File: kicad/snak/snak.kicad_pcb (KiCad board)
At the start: 2 copper layers, 115.6 x 99.6 mm, 70 parts

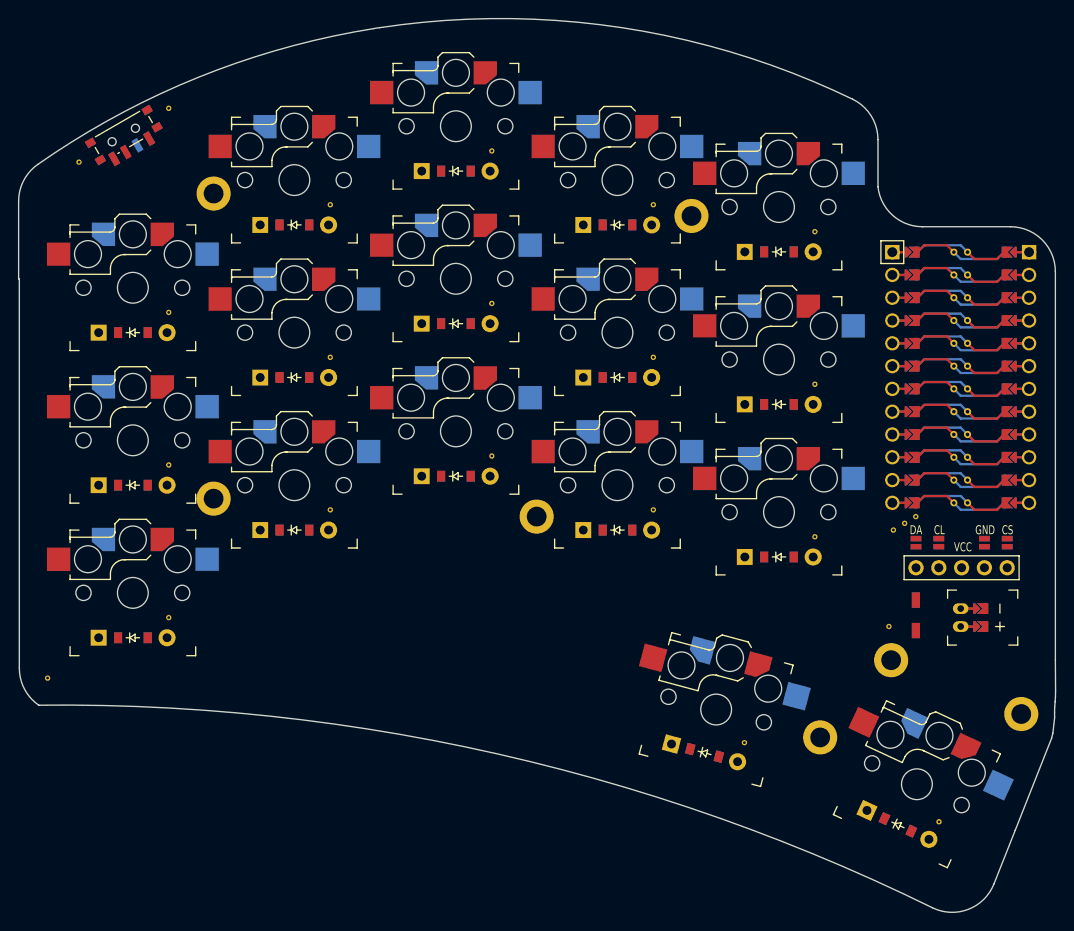
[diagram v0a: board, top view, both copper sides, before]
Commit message: changed the top and bottom curves to a single polygon
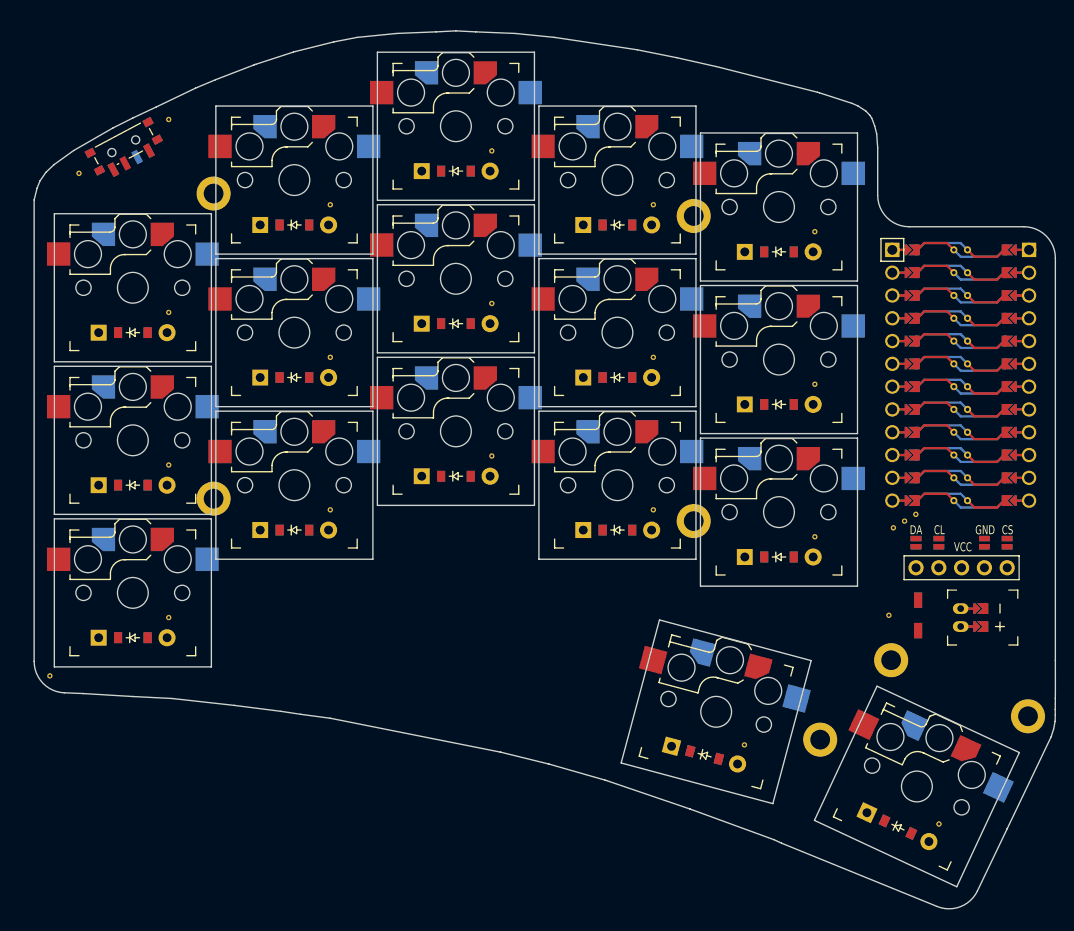
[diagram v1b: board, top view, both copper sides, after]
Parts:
- removed the REF** at (184.8, 93.0)
- removed the REF** at (168.2, 116.7)
- removed the REF** at (186.0, 92.2)
- removed the REF** at (189.8, 125.5)
- removed the REF** at (104.0, 46.0)
- removed the REF** at (94.0, 52.0)
- removed the REF** at (90.5, 109.5)
- removed the REF** at (184.2, 103.8)
- removed the REF** at (187.2, 91.5)
- added REF**: VIA-0.6mm, VIA-0.6mm, F.Cu at (184.8, 92.8)
- added REF**: VIA-0.6mm, VIA-0.6mm, F.Cu at (168.2, 116.9)
- added REF**: VIA-0.6mm, VIA-0.6mm, F.Cu at (186.0, 92.0)
- added REF**: VIA-0.6mm, VIA-0.6mm, F.Cu at (189.8, 125.8)
- added REF**: VIA-0.6mm, VIA-0.6mm, F.Cu at (104.0, 47.2)
- added REF**: VIA-0.6mm, VIA-0.6mm, F.Cu at (94.0, 53.2)
- added REF**: VIA-0.6mm, VIA-0.6mm, F.Cu at (90.8, 109.2)
- added REF**: VIA-0.6mm, VIA-0.6mm, F.Cu at (184.2, 102.5)
- added REF**: VIA-0.6mm, VIA-0.6mm, F.Cu at (187.2, 91.2)
- moved H4 17.5 mm to (162.5, 92.0)
- moved SW1 1.25 mm to (99.0, 50.2), turned to 118 degrees
- moved H7 0.79 mm to (199.8, 113.8)
- moved ? 0.25 mm to (187.5, 102.5)
- moved D16 0.25 mm to (163.7, 118.1)
- moved D17 0.25 mm to (185.3, 126.1)
- moved H3 0.25 mm to (162.5, 58.0)
- moved H5 0.25 mm to (176.6, 116.4)
- moved MCU1 0.25 mm to (192.2, 75.8)
- moved S16 0.25 mm to (165.0, 113.2)
- moved S17 0.25 mm to (187.4, 121.6)
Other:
- board size 115.6 x 99.6 mm -> 113.8 x 97.8 mm

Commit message: add via for oled gnd
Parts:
- added REF**: VIA-0.6mm, VIA-0.6mm, F.Cu at (194.9, 92.0)
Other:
- outline, holes or cut-outs redrawn
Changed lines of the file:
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@@
       (pad 1 thru_hole circle (at 0 0) (size 0.6 0.6) (drill 0.3) (layers *.Cu) (zone_connect 2) (net 20 "P7"))
+      )
+      (module VIA-0.6mm (layer F.Cu)
+      (at 194.9 92 0)
+      (fp_text reference REF** (at 0 1.4) (layer F.SilkS) hide (effects (font (size 1 1) (thickness 0.15))))
+      (fp_text value VIA-0.6mm (at 0 -1.4) (layer F.Fab) hide (effects (font (size 1 1) (thickness 0.15))))
+      (pad 1 thru_hole circle (at 0 0) (size 0.6 0.6) (drill 0.3) (layers *.Cu) (zone_connect 2) (net 2 "GND"))
       )
             (module PG1350 (layer F.Cu)
@@
 (gr_arc (start 145.45718132399764 122.4562241087232) (end 146.41926002399765 119.0910488087232) (angle -2.100604721951811) (layer Edge.Cuts) (width 0.15))
 (gr_arc (start 140.2553549312661 121.17331056590517) (end 141.09343903126612 117.77513236590516) (angle -2.5939778102701183) (layer Edge.Cuts) (width 0.15))
-(gr_line (start 91.25 108.25) (end 108.75 108.25) (angle 90) (layer Edge.Cuts) (width 0.15))
-(gr_line (start 108.75 108.25) (end 108.75 91.75) (angle 90) (layer Edge.Cuts) (width 0.15))
-(gr_line (start 108.75 91.75) (end 91.25 91.75) (angle 90) (layer Edge.Cuts) (width 0.15))
-(gr_line (start 91.25 91.75) (end 91.25 108.25) (angle 90) (layer Edge.Cuts) (width 0.15))
-(gr_line (start 91.25 91.25) (end 108.75 91.25) (angle 90) (layer Edge.Cuts) (width 0.15))
-(gr_line (start 108.75 91.25) (end 108.75 74.75) (angle 90) (layer Edge.Cuts) (width 0.15))
-(gr_line (start 108.75 74.75) (end 91.25 74.75) (angle 90) (layer Edge.Cuts) (width 0.15))
-(gr_line (start 91.25 74.75) (end 91.25 91.25) (angle 90) (layer Edge.Cuts) (width 0.15))
-(gr_line (start 91.25 74.25) (end 108.75 74.25) (angle 90) (layer Edge.Cuts) (width 0.15))
-(gr_line (start 108.75 74.25) (end 108.75 57.75) (angle 90) (layer Edge.Cuts) (width 0.15))
-(gr_line (start 108.75 57.75) (end 91.25 57.75) (angle 90) (layer Edge.Cuts) (width 0.15))
-(gr_line (start 91.25 57.75) (end 91.25 74.25) (angle 90) (layer Edge.Cuts) (width 0.15))
-(gr_line (start 109.25 96.25) (end 126.75 96.25) (angle 90) (layer Edge.Cuts) (width 0.15))
-(gr_line (start 126.75 96.25) (end 126.75 79.75) (angle 90) (layer Edge.Cuts) (width 0.15))
-(gr_line (start 126.75 79.75) (end 109.25 79.75) (angle 90) (layer Edge.Cuts) (width 0.15))
-(gr_line (start 109.25 79.75) (end 109.25 96.25) (angle 90) (layer Edge.Cuts) (width 0.15))
-(gr_line (start 109.25 79.25) (end 126.75 79.25) (angle 90) (layer Edge.Cuts) (width 0.15))
-(gr_line (start 126.75 79.25) (end 126.75 62.75) (angle 90) (layer Edge.Cuts) (width 0.15))
-(gr_line (start 126.75 62.75) (end 109.25 62.75) (angle 90) (layer Edge.Cuts) (width 0.15))
-(gr_line (start 109.25 62.75) (end 109.25 79.25) (angle 90) (layer Edge.Cuts) (width 0.15))
-(gr_line (start 109.25 62.25) (end 126.75 62.25) (angle 90) (layer Edge.Cuts) (width 0.15))
-(gr_line (start 126.75 62.25) (end 126.75 45.75) (angle 90) (layer Edge.Cuts) (width 0.15))
-(gr_line (start 126.75 45.75) (end 109.25 45.75) (angle 90) (layer Edge.Cuts) (width 0.15))
-(gr_line (start 109.25 45.75) (end 109.25 62.25) (angle 90) (layer Edge.Cuts) (width 0.15))
-(gr_line (start 127.25 90.25) (end 144.75 90.25) (angle 90) (layer Edge.Cuts) (width 0.15))
-(gr_line (start 144.75 90.25) (end 144.75 73.75) (angle 90) (layer Edge.Cuts) (width 0.15))
-(gr_line (start 144.75 73.75) (end 127.25 73.75) (angle 90) (layer Edge.Cuts) (width 0.15))
-(gr_line (start 127.25 73.75) (end 127.25 90.25) (angle 90) (layer Edge.Cuts) (width 0.15))
-(gr_line (start 127.25 73.25) (end 144.75 73.25) (angle 90) (layer Edge.Cuts) (width 0.15))
-(gr_line (start 144.75 73.25) (end 144.75 56.75) (angle 90) (layer Edge.Cuts) (width 0.15))
-(gr_line (start 144.75 56.75) (end 127.25 56.75) (angle 90) (layer Edge.Cuts) (width 0.15))
-(gr_line (start 127.25 56.75) (end 127.25 73.25) (angle 90) (layer Edge.Cuts) (width 0.15))
-(gr_line (start 127.25 56.25) (end 144.75 56.25) (angle 90) (layer Edge.Cuts) (width 0.15))
-(gr_line (start 144.75 56.25) (end 144.75 39.75) (angle 90) (layer Edge.Cuts) (width 0.15))
-(gr_line (start 144.75 39.75) (end 127.25 39.75) (angle 90) (layer Edge.Cuts) (width 0.15))
-(gr_line (start 127.25 39.75) (end 127.25 56.25) (angle 90) (layer Edge.Cuts) (width 0.15))
-(gr_line (start 145.25 96.25) (end 162.75 96.25) (angle 90) (layer Edge.Cuts) (width 0.15))
-(gr_line (start 162.75 96.25) (end 162.75 79.75) (angle 90) (layer Edge.Cuts) (width 0.15))
-(gr_line (start 162.75 79.75) (end 145.25 79.75) (angle 90) (layer Edge.Cuts) (width 0.15))
-(gr_line (start 145.25 79.75) (end 145.25 96.25) (angle 90) (layer Edge.Cuts) (width 0.15))
-(gr_line (start 145.25 79.25) (end 162.75 79.25) (angle 90) (layer Edge.Cuts) (width 0.15))
-(gr_line (start 162.75 79.25) (end 162.75 62.75) (angle 90) (layer Edge.Cuts) (width 0.15))
-(gr_line (start 162.75 62.75) (end 145.25 62.75) (angle 90) (layer Edge.Cuts) (width 0.15))
-(gr_line (start 145.25 62.75) (end 145.25 79.25) (angle 90) (layer Edge.Cuts) (width 0.15))
-(gr_line (start 145.25 62.25) (end 162.75 62.25) (angle 90) (layer Edge.Cuts) (width 0.15))
-(gr_line (start 162.75 62.25) (end 162.75 45.75) (angle 90) (layer Edge.Cuts) (width 0.15))
-(gr_line (start 162.75 45.75) (end 145.25 45.75) (angle 90) (layer Edge.Cuts) (width 0.15))
-(gr_line (start 145.25 45.75) (end 145.25 62.25) (angle 90) (layer Edge.Cuts) (width 0.15))
-(gr_line (start 163.25 99.25) (end 180.75 99.25) (angle 90) (layer Edge.Cuts) (width 0.15))
-(gr_line (start 180.75 99.25) (end 180.75 82.75) (angle 90) (layer Edge.Cuts) (width 0.15))
-(gr_line (start 180.75 82.75) (end 163.25 82.75) (angle 90) (layer Edge.Cuts) (width 0.15))
-(gr_line (start 163.25 82.75) (end 163.25 99.25) (angle 90) (layer Edge.Cuts) (width 0.15))
-(gr_line (start 163.25 82.25) (end 180.75 82.25) (angle 90) (layer Edge.Cuts) (width 0.15))
-(gr_line (start 180.75 82.25) (end 180.75 65.75) (angle 90) (layer Edge.Cuts) (width 0.15))
-(gr_line (start 180.75 65.75) (end 163.25 65.75) (angle 90) (layer Edge.Cuts) (width 0.15))
-(gr_line (start 163.25 65.75) (end 163.25 82.25) (angle 90) (layer Edge.Cuts) (width 0.15))
-(gr_line (start 163.25 65.25) (end 180.75 65.25) (angle 90) (layer Edge.Cuts) (width 0.15))
-(gr_line (start 180.75 65.25) (end 180.75 48.75) (angle 90) (layer Edge.Cuts) (width 0.15))
-(gr_line (start 180.75 48.75) (end 163.25 48.75) (angle 90) (layer Edge.Cuts) (width 0.15))
-(gr_line (start 163.25 48.75) (end 163.25 65.25) (angle 90) (layer Edge.Cuts) (width 0.15))
-(gr_line (start 154.4128919 118.9542214) (end 171.3165939 123.4835547) (angle 90) (layer Edge.Cuts) (width 0.15))
-(gr_line (start 171.3165939 123.4835547) (end 175.5871081 107.5457786) (angle 90) (layer Edge.Cuts) (width 0.15))
-(gr_line (start 175.5871081 107.5457786) (end 158.6834061 103.0164453) (angle 90) (layer Edge.Cuts) (width 0.15))
-(gr_line (start 158.6834061 103.0164453) (end 154.4128919 118.9542214) (angle 90) (layer Edge.Cuts) (width 0.15))
-(gr_line (start 175.95126100000002 125.35200309999998) (end 191.8116473 132.74782259999998) (angle 90) (layer Edge.Cuts) (width 0.15))
-(gr_line (start 191.8116473 132.74782259999998) (end 198.7848486 117.79374409999998) (angle 90) (layer Edge.Cuts) (width 0.15))
-(gr_line (start 198.7848486 117.79374409999998) (end 182.92446230000002 110.39792459999998) (angle 90) (layer Edge.Cuts) (width 0.15))
-(gr_line (start 182.92446230000002 110.39792459999998) (end 175.95126100000002 125.35200309999998) (angle 90) (layer Edge.Cuts) (width 0.15))
 (gr_line (start 91.25 108.25) (end 108.75 108.25) (angle 90) (layer Eco1.User) (width 0.15))
 (gr_line (start 108.75 108.25) (end 108.75 91.75) (angle 90) (layer Eco1.User) (width 0.15))

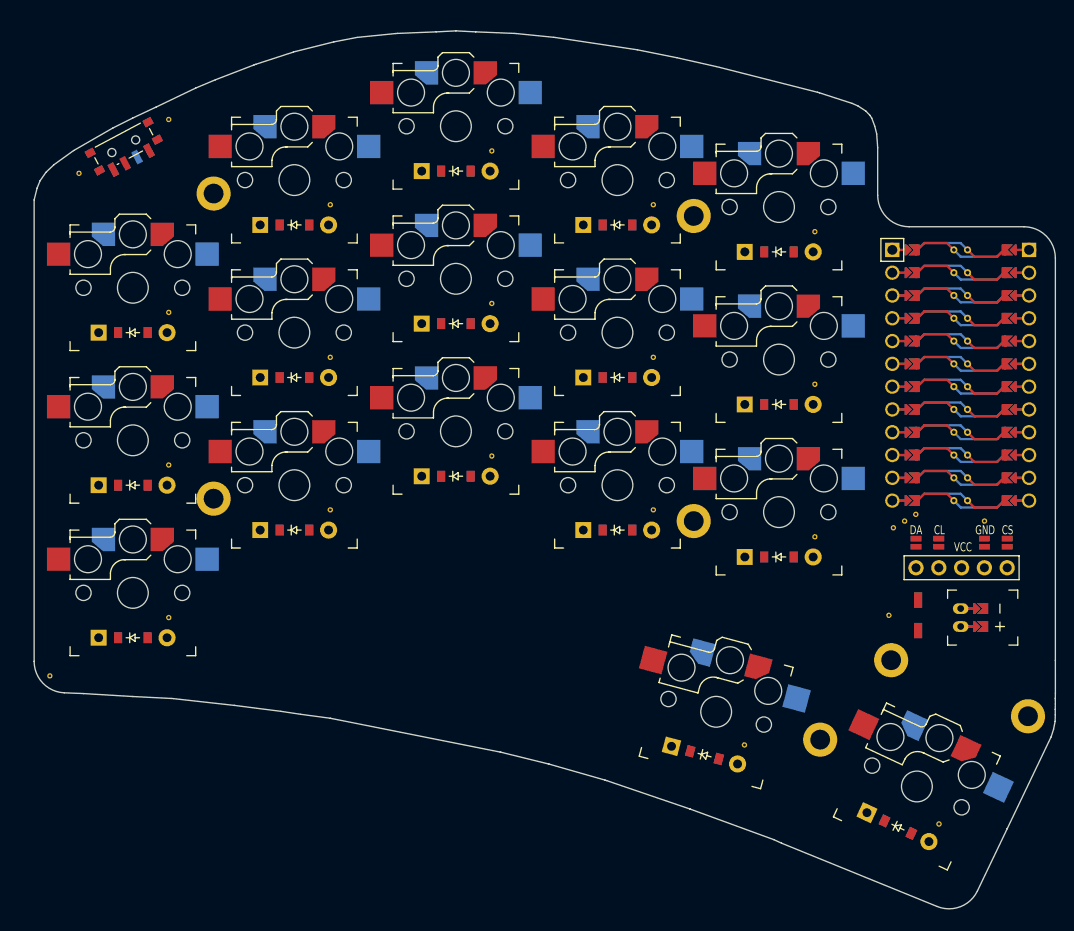
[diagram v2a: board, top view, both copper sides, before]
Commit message: update config with circle intersect
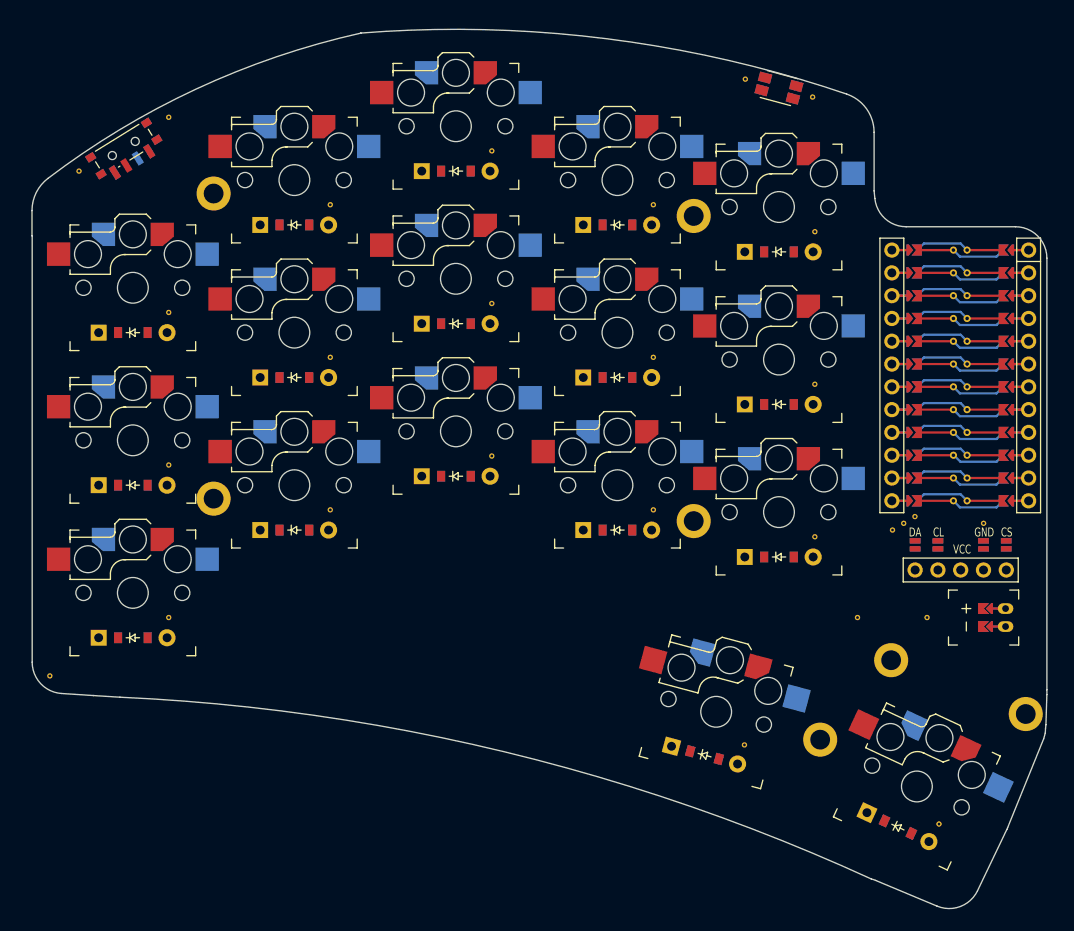
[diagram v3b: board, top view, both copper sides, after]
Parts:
- removed ?: , Button_Switch_SMD:SW_SPST_B3U-1000P
- removed the REF** at (184.8, 92.8)
- removed the REF** at (186.0, 92.0)
- removed the REF** at (104.0, 47.2)
- removed the REF** at (94.0, 53.2)
- removed the REF** at (184.2, 102.5)
- removed the REF** at (187.2, 91.2)
- removed the REF** at (194.9, 92.0)
- added REF**: VIA-0.6mm, VIA-0.6mm, F.Cu at (184.7, 93.0)
- added REF**: VIA-0.6mm, VIA-0.6mm, F.Cu at (185.9, 92.2)
- added REF**: VIA-0.6mm, VIA-0.6mm, F.Cu at (175.8, 44.8)
- added REF**: VIA-0.6mm, VIA-0.6mm, F.Cu at (168.2, 42.8)
- added REF**: VIA-0.6mm, VIA-0.6mm, F.Cu at (104.0, 47.0)
- added REF**: VIA-0.6mm, VIA-0.6mm, F.Cu at (94.0, 53.0)
- added REF**: VIA-0.6mm, VIA-0.6mm, F.Cu at (188.5, 102.8)
- added REF**: VIA-0.6mm, VIA-0.6mm, F.Cu at (180.8, 102.8)
- added REF**: VIA-0.6mm, VIA-0.6mm, F.Cu at (187.2, 91.5)
- added REF**: VIA-0.6mm, VIA-0.6mm, F.Cu at (194.8, 92.2)
- added SW2: , power_switch, F.Cu at (99.0, 50.5)
- MCU1: footprint ProMicro -> nice_nano
- SW1: footprint power_switch -> sw_reset_side
- moved SW1 73.3 mm to (172.0, 43.8), turned to 75 degrees
- moved JST1 5.00 mm to (197.2, 102.8), turned to -90 degrees
- moved MCU1 1.25 mm to (192.2, 74.5), turned to 0 degrees
- moved H7 0.35 mm to (199.5, 113.5)
- moved DISP1 0.27 mm to (192.2, 80.8)
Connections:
- D1 pad 1: P19 -> P16
- D10 pad 1: P19 -> P16
- D11 pad 1: P20 -> P14
- D12 pad 1: P21 -> P15
- D13 pad 1: P19 -> P16
- D14 pad 1: P20 -> P14
- D15 pad 1: P21 -> P15
- D16 pad 1: P16 -> P10
- D17 pad 1: P16 -> P10
- D2 pad 1: P20 -> P14
- D3 pad 1: P21 -> P15
- D4 pad 1: P19 -> P16
- D5 pad 1: P20 -> P14
- D6 pad 1: P21 -> P15
- D7 pad 1: P19 -> P16
- D8 pad 1: P20 -> P14
- D9 pad 1: P21 -> P15
- MCU1 pad 1: RAW -> MCU1_1
- MCU1 pad 10: P14 -> MCU1_10
- MCU1 pad 11: P16 -> MCU1_11
- MCU1 pad 12: P10 -> MCU1_12
- MCU1 pad 13: P9 -> MCU1_13
- MCU1 pad 14: P8 -> MCU1_14
- MCU1 pad 15: P7 -> MCU1_15
- MCU1 pad 16: P6 -> MCU1_16
- MCU1 pad 17: P5 -> MCU1_17
- MCU1 pad 18: P4 -> MCU1_18
- MCU1 pad 19: P3 -> MCU1_19
- MCU1 pad 2: GND -> MCU1_2
- MCU1 pad 20: P2 -> MCU1_20
- MCU1 pad 21: GND -> MCU1_21
- MCU1 pad 22: GND -> MCU1_22
- MCU1 pad 23: P0 -> MCU1_23
- MCU1 pad 24: P1 -> MCU1_24
- MCU1 pad 3: RST -> MCU1_3
- MCU1 pad 4: VCC -> MCU1_4
- MCU1 pad 5: P21 -> MCU1_5
- MCU1 pad 6: P20 -> MCU1_6
- MCU1 pad 7: P19 -> MCU1_7
- MCU1 pad 8: P18 -> MCU1_8
- MCU1 pad 9: P15 -> MCU1_9
- REF** pad 1: P14 -> P3
- REF** pad 1: P10 -> P4
- S16 pad 1: P14 -> P3
- S17 pad 1: P10 -> P4
- SW1 pad 1: (no net) -> GND
- SW1 pad 2: pos -> RST
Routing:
- net (no net): track 0.00 -> 345.6 mm
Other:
- board size 113.8 x 97.8 mm -> 113.1 x 98 mm
